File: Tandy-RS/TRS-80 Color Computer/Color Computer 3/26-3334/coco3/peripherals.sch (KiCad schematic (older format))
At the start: 50 parts, among them IC7 SC77526, IC8 SC77527P, Q1 2N6123

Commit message: finished GIME section
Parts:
- removed RP?: 4.7K, Resistor_THT:R_Array_SIP10, symbol Device:R_Network09_US
- added C47, C48: .1uF, Capacitor_THT:C_Disc_D4.7mm_W2.5mm_P5.00mm, symbol Device:C_Small
- added IC14: 74LS30, Package_DIP:DIP-14_W7.62mm_Socket, symbol 74xx:74LS30
- gave numbers to parts that had none: 15
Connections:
- net labels added: IL1, PA0, PA1, PA2, PA3, PA4, PA5, PA6
- wire segments 316 -> 321

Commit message: cleaned up the peripherals sheet a little
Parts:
- removed C1004, C1005: .1uF, Capacitor_THT:C_Disc_D4.7mm_W2.5mm_P5.00mm, symbol Device:C_Small
- removed CR1001: 1KF20-04, Diode_THT:D_A-405_P10.16mm_Horizontal, symbol Device:D_Small
- removed K1001: HB1-DC5V-H62, coco2:HB1-DC5V-H62_W7.62mm, symbol coco2:HB1-DC5V-H62
- added C18, C19, C22, C23: 1800pF, Capacitor_THT:C_Disc_D4.7mm_W2.5mm_P5.00mm, symbol Device:C_Small
- added D10, D8, D9: 1KF20-04, Diode_THT:D_A-405_P10.16mm_Horizontal, symbol Device:D_Small
- added FB10, FB9: Ferrite_Bead_Small, coco2:ferrite_bead, symbol Device:Ferrite_Bead_Small
- renumbered C1003 to C49, CR1002 to D11, J1002 to JK1, J1003 to JK2, R1001 to R13, K1002 to RY1
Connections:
- net labels added: JOY2, JOY3, SND_IN_2
- net labels removed: CART_SND, CASSOUT, CASS_PIN1, CASS_PIN3, LSW, RSW
- wire segments 321 -> 324
- no-connect marks 6 -> 5
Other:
- note added: "RY1 is not the original relay\nbecause the original because \nthe original is no longer made."
- note removed: "K2 is not the original relay\nbut it was added in parallel\nwith the original because the\noriginal is no longer made."
- moved on the sheet: C14, C15, C16, C17, C25, C47, C48, C49, D11, D5, D6, D7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

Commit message: finished peripherals sheet
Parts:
- removed C1006: 33pF, Capacitor_THT:C_Rect_L7.2mm_W3.0mm_P5.00mm_FKS2_FKP2_MKS2_MKP2, symbol Device:C_Small
- added IC15: 74LS04, Package_DIP:DIP-14_W7.62mm_Socket, symbol 74xx:74LS04
- renumbered C1002 to C7, U1002 to IC4
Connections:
- net RP1-4 is gone; now on net SELB: IC5.19 (CB2)
- net HI: no longer IC5.24 (CS1)
- net A5: now reaches IC4.24 (CS1)
- net A5: now also IC15.3
- net HI_LO renamed PA7
- net ~FS renamed ~VSYNC
- net ~HS renamed ~HSYNC
- new net: IC15.4, IC5.24 (CS1)
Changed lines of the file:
@@
 Wire Bus Line
 	1800 2250 1800 2150
-Wire Bus Line
-	1800 2150 1500 2150
-Text HLabel 1500 2150 0    50   Input ~ 0
+Text HLabel 1400 2150 0    50   Input ~ 0
 A[0..15]
 Wire Wire Line
@@
 Wire Wire Line
 	1100 1250 2450 1250
-Wire Wire Line
-	2450 2550 2350 2550
-Wire Wire Line
-	2350 2550 2350 2650
-Wire Wire Line
-	2350 2650 2450 2650
-Wire Wire Line
-	2100 2550 2350 2550
-Connection ~ 2350 2550
-Text Label 2100 2550 2    50   ~ 0
+Text Label 1950 2450 2    50   ~ 0
 HI
-Text HLabel 3650 2150 2    50   Input ~ 0
-~HS
-Text HLabel 3650 3450 2    50   Input ~ 0
-~FS
-Wire Wire Line
-	3450 2150 3650 2150
-Wire Wire Line
-	3650 3450 3450 3450
 Wire Wire Line
 	2950 3850 2950 3950
@@
 AR Path="/60273794/60E357B9" Ref="C?"  Part="1"
 AR Path="/602A51A8/60E357B9" Ref="C?"  Part="1"
-AR Path="/603CF7B8/60E357B9" Ref="C1002"  Part="1"
-F 0 "C1002" V 2750 850 50  0000 C CNN
+AR Path="/603CF7B8/60E357B9" Ref="C7"  Part="1"
+F 0 "C7" V 2750 850 50  0000 C CNN
 F 1 ".1uF" V 2500 850 50  0000 C CNN
 F 2 "Capacitor_THT:C_Disc_D4.7mm_W2.5mm_P5.00mm" H 2600 850 50  0001 C CNN
@@
 Wire Wire Line
 	2150 4400 2550 4400
-Text Label 3650 3550 0    50   ~ 0
-RP1-4
-Wire Wire Line
-	3650 3550 3450 3550
 Text HLabel 4450 7000 2    50   Input ~ 0
 ~CART
@@
 	1    0    0    -1
 $EndComp
-Wire Wire Line
-	3000 7400 3000 7550
 $Comp
 L power:+5V #PWR?
@@
 CASS_DATA_IN
 Text Label 6650 4950 0    50   ~ 0
-HI_LO
+PA7
 Wire Wire Line
 	6500 4950 6650 4950
-Text Label 3600 1950 0    50   ~ 0
-HI_LO
-Wire Wire Line
-	3450 1950 3600 1950
+Text Label 3450 1950 0    50   ~ 0
+PA7
 Wire Wire Line
 	3450 3150 4000 3150
@@
 ECLK
 Wire Wire Line
-	1500 6600 1750 6600
-$Comp
-L Device:C_Small C?
-U 1 1 60E6536C
-P 1750 6900
-AR Path="/60273794/60E6536C" Ref="C?"  Part="1"
-AR Path="/603CF7B8/60E6536C" Ref="C1006"  Part="1"
-F 0 "C1006" H 1658 6854 50  0000 R CNN
-F 1 "33pF" H 1658 6945 50  0000 R CNN
-F 2 "Capacitor_THT:C_Rect_L7.2mm_W3.0mm_P5.00mm_FKS2_FKP2_MKS2_MKP2" H 1750 6900 50  0001 C CNN
-F 3 "https://product.tdk.com/info/en/catalog/datasheets/leadmlcc_halogenfree_fa150_en.pdf?ref_disty=digikey" H 1750 6900 50  0001 C CNN
-F 4 "digikey" H 1750 6900 50  0001 C CNN "Vendor"
-F 5 "445-180775-1-ND" H 1750 6900 50  0001 C CNN "Vendor part#"
-F 6 "FA28NP01H330JNU06" H 1750 6900 50  0001 C CNN "Manufacturer part#"
-	1    1750 6900
-	-1   0    0    1
-$EndComp
-Wire Wire Line
-	1750 6600 1750 6800
-Connection ~ 1750 6600
-Wire Wire Line
-	1750 6600 2500 6600
-Wire Wire Line
-	1750 7550 3000 7550
-Connection ~ 3000 7550
-Wire Wire Line
-	3000 7550 3000 7650
-Wire Wire Line
-	1750 7000 1750 7550
-Wire Wire Line
 	2500 6800 2350 6800
 Wire Wire Line
@@
 NoConn ~ 3500 6800
 $Comp
-L Interface:6821 U1002
+L Interface:6821 IC4
 U 1 1 60B3AA45
 P 3000 6000
-F 0 "U1002" H 2750 7400 50  0000 C CNN
+F 0 "IC4" H 2750 7400 50  0000 C CNN
 F 1 "6821" H 3250 7350 50  0000 C CNN
 F 2 "Package_DIP:DIP-40_W15.24mm_Socket" H 3050 4650 50  0001 L CNN
@@
 	1    0    0    -1
 $EndComp
-Text HLabel 1900 2750 0    50   Input ~ 0
+Text HLabel 1800 2850 0    50   Input ~ 0
 PIA_~CS2
 Wire Wire Line
-	1900 2750 2450 2750
-Text Label 2300 2750 2    50   ~ 0
+	1800 2850 2350 2850
+Text Label 2200 2850 2    50   ~ 0
 PIA_~CS2
-Text Label 2350 6300 2    50   ~ 0
+Text Label 2300 6400 2    50   ~ 0
 PIA_~CS2
-Wire Wire Line
-	2500 6300 2350 6300
 Text Label 3450 1250 0    50   ~ 0
 PA0
@@
 Wire Wire Line
 	7900 7150 7900 7650
+Connection ~ 7900 7650
+Entry Wire Line
+	1800 6200 1700 6300
+Text HLabel 1400 6300 0    50   Input ~ 0
+A[0..15]
+Wire Bus Line
+	1700 6300 1400 6300
+Wire Wire Line
+	2300 6400 2400 6400
+Wire Wire Line
+	2400 6400 2400 6300
+Wire Wire Line
+	2400 6300 2500 6300
+Wire Wire Line
+	2500 6200 1800 6200
+Text Label 2350 6200 0    50   ~ 0
+A5
+Wire Wire Line
+	1500 6600 2500 6600
+Wire Wire Line
+	3000 7400 3000 7650
+Text HLabel 3600 3450 2    50   Input ~ 0
+~VSYNC
+Wire Wire Line
+	3600 3450 3450 3450
+Text HLabel 3650 2150 2    50   Input ~ 0
+~HSYNC
+Wire Wire Line
+	3450 2150 3650 2150
+Text Label 3650 3550 0    50   ~ 0
+SELB
+Wire Wire Line
+	3450 3550 3650 3550
+Wire Wire Line
+	2450 2750 2350 2750
+Wire Wire Line
+	2350 2750 2350 2850
+$Comp
+L 74xx:74LS04 IC?
+U 2 1 63B9CBA3
+P 1850 2600
+AR Path="/63B9CBA3" Ref="IC?"  Part="7"
+AR Path="/61257512/63B9CBA3" Ref="IC?"  Part="4"
+AR Path="/603CF7B8/63B9CBA3" Ref="IC15"  Part="2"
+F 0 "IC15" H 1450 2500 50  0000 L CNN
+F 1 "74LS04" H 1600 2800 50  0000 L CNN
+F 2 "Package_DIP:DIP-14_W7.62mm_Socket" H 1850 2600 50  0001 C CNN
+F 3 "https://www.ti.com/general/docs/suppproductinfo.tsp?distId=10&gotoUrl=https%3A%2F%2Fwww.ti.com%2Flit%2Fgpn%2Fsn74ls04" H 1850 2600 50  0001 C CNN
+F 4 "digikey" H 1850 2600 50  0001 C CNN "Vendor"
+F 5 "296-1629-5-ND" H 1850 2600 50  0001 C CNN "Vendor part#"
+F 6 "SN74LS04N" H 1850 2600 50  0001 C CNN "Manufacturer part#"
+	2    1850 2600
+	1    0    0    -1
+$EndComp
+Wire Wire Line
+	2350 2450 2350 2550
+Wire Wire Line
+	2350 2550 2450 2550
+Wire Wire Line
+	1950 2450 2350 2450
+Entry Wire Line
+	1550 2150 1450 2250
+Wire Wire Line
+	1450 2250 1450 2600
+Wire Wire Line
+	1450 2600 1550 2600
+Text Label 1300 2600 2    50   ~ 0
+A5
+Wire Wire Line
+	1300 2600 1450 2600
+Connection ~ 1450 2600
+Wire Wire Line
+	2150 2600 2250 2600
+Wire Wire Line
+	2250 2600 2250 2650
+Wire Wire Line
+	2250 2650 2450 2650
+Wire Bus Line
+	1400 2150 1800 2150
 Wire Bus Line
 	1000 1150 1000 5400
-Connection ~ 7900 7650
 $EndSCHEMATC

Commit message: added some more to the video sheet
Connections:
- net SND_OUT renamed SOUND
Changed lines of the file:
@@
 	4750 7100 4750 5700
 Text HLabel 5350 6000 0    50   Output ~ 0
-SND_OUT
+SOUND
 Wire Wire Line
 	5500 6000 5450 6000

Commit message: -swapped 5v to 8v inthe video section. -swapped collector and emitter connections for Q1 -sourced more coponents -started pcb
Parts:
- Q1: symbol Transistor_BJT:2N3055 -> Device:Q_NPN_BCE
- renumbered J1001 to CN2
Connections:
- net +SALT_VIN: now also Q1.2 (C); no longer Q1.3 (C)
- net at R19.2, R20.1: now also Q1.3 (E); no longer Q1.2 (E)
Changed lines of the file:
@@
 $EndDescr
 $Comp
-L Transistor_BJT:2N3055 Q?
+L Device:Q_NPN_BCE Q?
 U 1 1 60A8718E
 P 9700 1850
@@
 F 7 "ED40DT" H 2950 2450 50  0001 C CNN "Manufacturer part#"
 	1    2950 2450
-	1    0    0    -1
-$EndComp
-$Comp
-L Connector:Conn_01x16_Female J1001
-U 1 1 60B58FEF
-P 5000 1850
-F 0 "J1001" H 5028 1826 50  0000 L CNN
-F 1 "Conn_01x16_Female" H 5028 1735 50  0001 L CNN
-F 2 "Connector_PinHeader_2.54mm:PinHeader_1x16_P2.54mm_Vertical" H 5000 1850 50  0001 C CNN
-F 3 "https://www.te.com/commerce/DocumentDelivery/DDEController?Action=srchrtrv&DocNm=520415&DocType=Customer+Drawing&DocLang=English" H 5000 1850 50  0001 C CNN
-F 4 "digikey" H 5000 1850 50  0001 C CNN "Vendor"
-F 5 "A144434-ND" H 5000 1850 50  0001 C CNN "Vendor part#"
-F 6 "6-520415-6" H 5000 1850 50  0001 C CNN "Manufacturer part#"
-	1    5000 1850
 	1    0    0    -1
 $EndComp
@@
 Wire Wire Line
 	2250 2650 2450 2650
+$Comp
+L Connector:Conn_01x16_Female CN2
+U 1 1 60B58FEF
+P 5000 1850
+F 0 "CN2" H 5028 1826 50  0000 L CNN
+F 1 "Conn_01x16_Female" H 5028 1735 50  0001 L CNN
+F 2 "Connector_PinHeader_2.54mm:PinHeader_1x16_P2.54mm_Vertical" H 5000 1850 50  0001 C CNN
+F 3 "https://www.te.com/commerce/DocumentDelivery/DDEController?Action=srchrtrv&DocNm=520415&DocType=Customer+Drawing&DocLang=English" H 5000 1850 50  0001 C CNN
+F 4 "digikey" H 5000 1850 50  0001 C CNN "Vendor"
+F 5 "A144434-ND" H 5000 1850 50  0001 C CNN "Vendor part#"
+F 6 "6-520415-6" H 5000 1850 50  0001 C CNN "Manufacturer part#"
+	1    5000 1850
+	1    0    0    -1
+$EndComp
 Wire Bus Line
 	1400 2150 1800 2150

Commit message: -added some 3d models -fixed ferrite bead footprints
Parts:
- FB10, FB6, FB7, FB8, FB9: value Ferrite_Bead_Small -> (none); footprint coco2:ferrite_bead -> coco2:FB_28L0138-10R-10; Manufacturer part# 2743007111 -> 28L0138-10R-10; Vendor part# 1934-1364-ND -> 240-2438-1-ND
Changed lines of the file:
@@
 AR Path="/603CF7B8/611ED7B5" Ref="FB7"  Part="1"
 F 0 "FB7" V 11750 5550 50  0000 L CNN
-F 1 "Ferrite_Bead_Small" H 11700 5555 50  0001 L CNN
-F 2 "coco2:ferrite_bead" V 11530 5600 50  0001 C CNN
-F 3 "http://www.fair-rite.com/wp-content/themes/fair-rite/print_product.php?pid=18608" H 11600 5600 50  0001 C CNN
+F 1 " " H 11700 5555 50  0001 L CNN
+F 2 "coco2:FB_28L0138-10R-10" V 11530 5600 50  0001 C CNN
+F 3 " https://media.digikey.com/pdf/Data%20Sheets/Laird%20Technologies/Ferrite_EMI_Cable_Cores.pdf" H 11600 5600 50  0001 C CNN
 F 4 "digikey" H 11600 5600 50  0001 C CNN "Vendor"
-F 5 "1934-1364-ND" H 11600 5600 50  0001 C CNN "Vendor part#"
-F 6 "2743007111" H 11600 5600 50  0001 C CNN "Manufacturer part#"
+F 5 "240-2438-1-ND" H 11600 5600 50  0001 C CNN "Vendor part#"
+F 6 "28L0138-10R-10" H 11600 5600 50  0001 C CNN "Manufacturer part#"
 	1    11600 5600
 	0    -1   -1   0
@@
 AR Path="/603CF7B8/61285B98" Ref="FB8"  Part="1"
 F 0 "FB8" H 11950 6250 50  0000 L CNN
-F 1 "Ferrite_Bead_Small" H 12200 6105 50  0001 L CNN
-F 2 "coco2:ferrite_bead" V 12030 6150 50  0001 C CNN
-F 3 "http://www.fair-rite.com/wp-content/themes/fair-rite/print_product.php?pid=18608" H 12100 6150 50  0001 C CNN
+F 1 " " H 12200 6105 50  0001 L CNN
+F 2 "coco2:FB_28L0138-10R-10" V 12030 6150 50  0001 C CNN
+F 3 " https://media.digikey.com/pdf/Data%20Sheets/Laird%20Technologies/Ferrite_EMI_Cable_Cores.pdf" H 12100 6150 50  0001 C CNN
 F 4 "digikey" H 12100 6150 50  0001 C CNN "Vendor"
-F 5 "1934-1364-ND" H 12100 6150 50  0001 C CNN "Vendor part#"
-F 6 "2743007111" H 12100 6150 50  0001 C CNN "Manufacturer part#"
+F 5 "240-2438-1-ND" H 12100 6150 50  0001 C CNN "Vendor part#"
+F 6 "28L0138-10R-10" H 12100 6150 50  0001 C CNN "Manufacturer part#"
 	1    12100 6150
 	1    0    0    -1
@@
 AR Path="/603CF7B8/60FAA0D8" Ref="FB6"  Part="1"
 F 0 "FB6" V 7500 6000 50  0000 L CNN
-F 1 "Ferrite_Bead_Small" H 7450 5955 50  0001 L CNN
-F 2 "coco2:ferrite_bead" V 7280 6000 50  0001 C CNN
-F 3 "http://www.fair-rite.com/wp-content/themes/fair-rite/print_product.php?pid=18608" H 7350 6000 50  0001 C CNN
+F 1 " " H 7450 5955 50  0001 L CNN
+F 2 "coco2:FB_28L0138-10R-10" V 7280 6000 50  0001 C CNN
+F 3 " https://media.digikey.com/pdf/Data%20Sheets/Laird%20Technologies/Ferrite_EMI_Cable_Cores.pdf" H 7350 6000 50  0001 C CNN
 F 4 "digikey" H 7350 6000 50  0001 C CNN "Vendor"
-F 5 "1934-1364-ND" H 7350 6000 50  0001 C CNN "Vendor part#"
-F 6 "2743007111" H 7350 6000 50  0001 C CNN "Manufacturer part#"
+F 5 "240-2438-1-ND" H 7350 6000 50  0001 C CNN "Vendor part#"
+F 6 "28L0138-10R-10" H 7350 6000 50  0001 C CNN "Manufacturer part#"
 	1    7350 6000
 	0    -1   -1   0
@@
 AR Path="/603CF7B8/6167C1CB" Ref="FB9"  Part="1"
 F 0 "FB9" V 12150 1200 50  0000 L CNN
-F 1 "Ferrite_Bead_Small" H 12450 1205 50  0001 L CNN
-F 2 "coco2:ferrite_bead" V 12280 1250 50  0001 C CNN
-F 3 "http://www.fair-rite.com/wp-content/themes/fair-rite/print_product.php?pid=18608" H 12350 1250 50  0001 C CNN
+F 1 " " H 12450 1205 50  0001 L CNN
+F 2 "coco2:FB_28L0138-10R-10" V 12280 1250 50  0001 C CNN
+F 3 " https://media.digikey.com/pdf/Data%20Sheets/Laird%20Technologies/Ferrite_EMI_Cable_Cores.pdf" H 12350 1250 50  0001 C CNN
 F 4 "digikey" H 12350 1250 50  0001 C CNN "Vendor"
-F 5 "1934-1364-ND" H 12350 1250 50  0001 C CNN "Vendor part#"
-F 6 "2743007111" H 12350 1250 50  0001 C CNN "Manufacturer part#"
+F 5 "240-2438-1-ND" H 12350 1250 50  0001 C CNN "Vendor part#"
+F 6 "28L0138-10R-10" H 12350 1250 50  0001 C CNN "Manufacturer part#"
 	1    12350 1250
 	0    1    1    0
@@
 AR Path="/603CF7B8/622CAFCF" Ref="FB10"  Part="1"
 F 0 "FB10" V 12150 3250 50  0000 L CNN
-F 1 "Ferrite_Bead_Small" H 12450 3255 50  0001 L CNN
-F 2 "coco2:ferrite_bead" V 12280 3300 50  0001 C CNN
-F 3 "http://www.fair-rite.com/wp-content/themes/fair-rite/print_product.php?pid=18608" H 12350 3300 50  0001 C CNN
+F 1 " " H 12450 3255 50  0001 L CNN
+F 2 "coco2:FB_28L0138-10R-10" V 12280 3300 50  0001 C CNN
+F 3 " https://media.digikey.com/pdf/Data%20Sheets/Laird%20Technologies/Ferrite_EMI_Cable_Cores.pdf" H 12350 3300 50  0001 C CNN
 F 4 "digikey" H 12350 3300 50  0001 C CNN "Vendor"
-F 5 "1934-1364-ND" H 12350 3300 50  0001 C CNN "Vendor part#"
-F 6 "2743007111" H 12350 3300 50  0001 C CNN "Manufacturer part#"
+F 5 "240-2438-1-ND" H 12350 3300 50  0001 C CNN "Vendor part#"
+F 6 "28L0138-10R-10" H 12350 3300 50  0001 C CNN "Manufacturer part#"
 	1    12350 3300
 	0    1    1    0

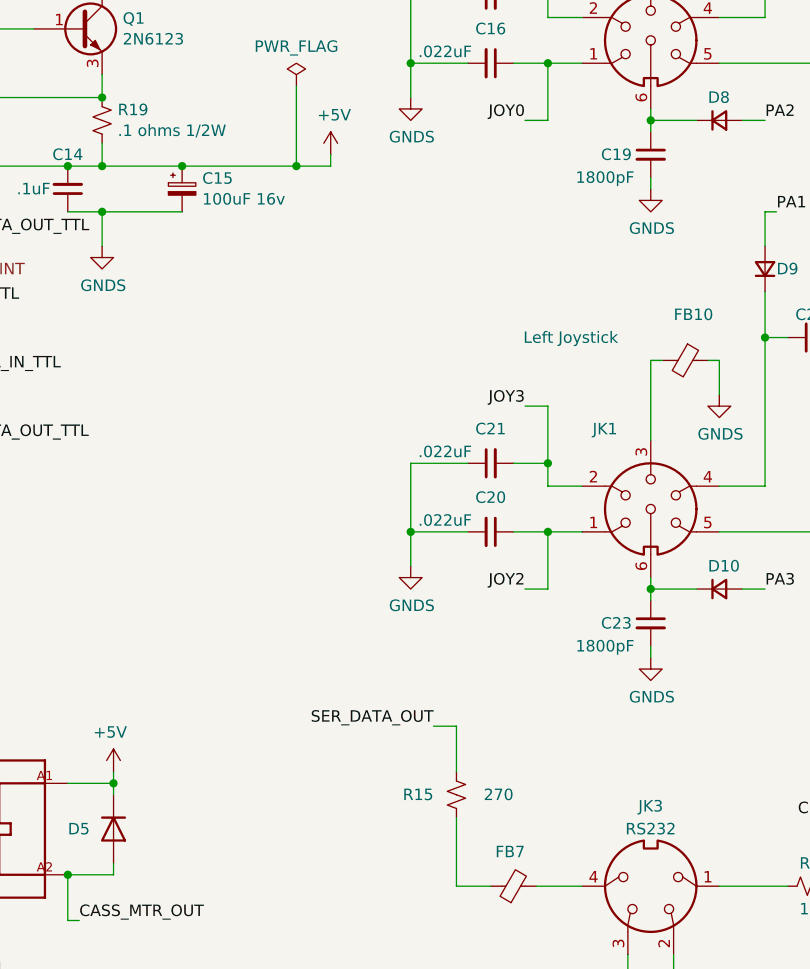
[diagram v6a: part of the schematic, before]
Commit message: -added CN4 CN5 and CN6 -placed all but one component in PCB
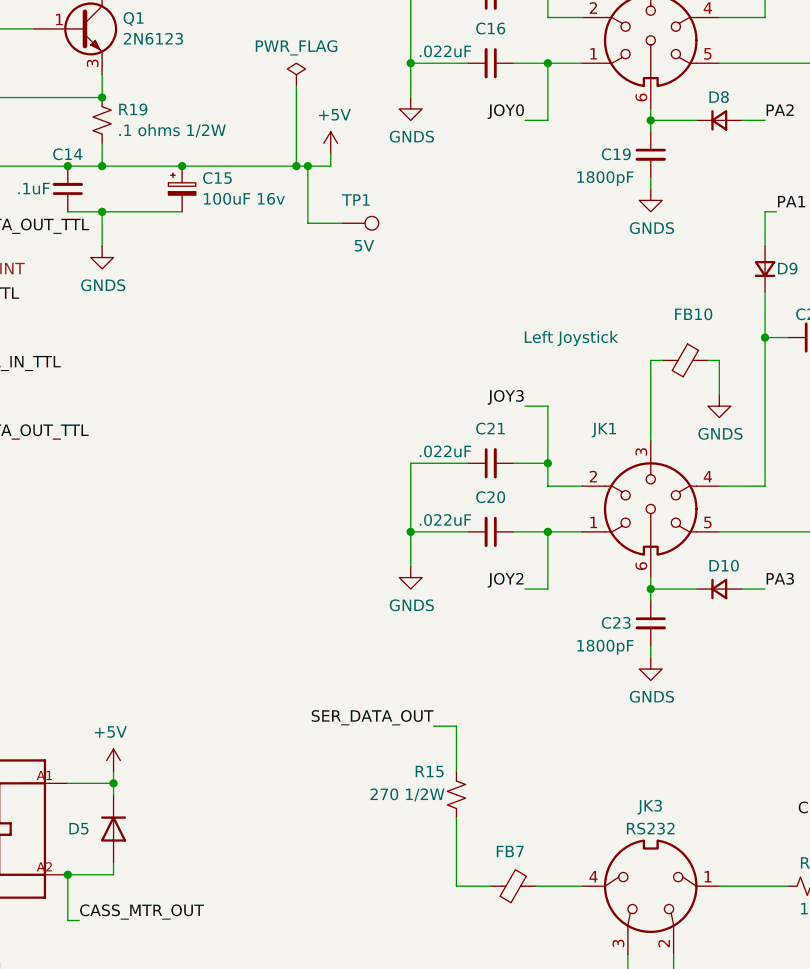
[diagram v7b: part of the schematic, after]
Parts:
- added TP1: 5V, TestPoint:TestPoint_Pad_3.0x3.0mm, symbol Connector:TestPoint
- R15: value 270 -> 270 1/2W; footprint Resistor_THT:R_Axial_DIN0207_L6.3mm_D2.5mm_P10.16mm_Horizontal -> Resistor_THT:R_Axial_DIN0204_L3.6mm_D1.6mm_P7.62mm_Horizontal; Manufacturer part# CF14JT270R -> SFR16S0002700JA500; Vendor part# CF14JT270RCT-ND -> BC4316CT-ND
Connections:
- net +5V: now also TP1.1
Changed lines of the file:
@@
 	10800 2400 10800 2450
 Wire Wire Line
-	10800 2450 10650 2450
+	10800 2450 10700 2450
 Connection ~ 10150 2450
 $Comp
@@
 AR Path="/60273794/61810AA1" Ref="R?"  Part="1"
 AR Path="/603CF7B8/61810AA1" Ref="R15"  Part="1"
-F 0 "R15" H 11450 5200 50  0000 L CNN
-F 1 "270" H 11100 5200 50  0000 L CNN
-F 2 "Resistor_THT:R_Axial_DIN0207_L6.3mm_D2.5mm_P10.16mm_Horizontal" H 11350 5200 50  0001 C CNN
-F 3 "https://www.seielect.com/catalog/sei-cf_cfm.pdf" H 11350 5200 50  0001 C CNN
+F 0 "R15" H 11400 5100 50  0000 L CNN
+F 1 "270 1/2W" H 11400 5200 50  0000 L CNN
+F 2 "Resistor_THT:R_Axial_DIN0204_L3.6mm_D1.6mm_P7.62mm_Horizontal" H 11350 5200 50  0001 C CNN
+F 3 "https://www.vishay.com/docs/28722/sfr16s25.pdf" H 11350 5200 50  0001 C CNN
 F 4 "digikey" H 11350 5200 50  0001 C CNN "Vendor"
-F 5 "CF14JT270RCT-ND" H 11350 5200 50  0001 C CNN "Vendor part#"
-F 6 "CF14JT270R" H 11350 5200 50  0001 C CNN "Manufacturer part#"
+F 5 "BC4316CT-ND" H 11350 5200 50  0001 C CNN "Vendor part#"
+F 6 "SFR16S0002700JA500" H 11350 5200 50  0001 C CNN "Manufacturer part#"
 	1    11350 5200
 	-1   0    0    1
@@
 	1    0    0    -1
 $EndComp
+$Comp
+L Connector:TestPoint TP?
+U 1 1 61407312
+P 10850 2700
+AR Path="/612A4892/61407312" Ref="TP?"  Part="1"
+AR Path="/603CF7B8/61407312" Ref="TP1"  Part="1"
+F 0 "TP1" V 10750 2700 50  0000 L CNN
+F 1 "5V" V 10950 2750 50  0000 L CNN
+F 2 "TestPoint:TestPoint_Pad_3.0x3.0mm" H 11050 2700 50  0001 C CNN
+F 3 "~" H 11050 2700 50  0001 C CNN
+	1    10850 2700
+	0    1    1    0
+$EndComp
+Wire Wire Line
+	10700 2700 10700 2450
+Wire Wire Line
+	10700 2700 10850 2700
 Wire Bus Line
 	1400 2150 1800 2150
 Wire Bus Line
 	1000 1150 1000 5400
+Connection ~ 10700 2450
+Wire Wire Line
+	10700 2450 10650 2450
 $EndSCHEMATC
